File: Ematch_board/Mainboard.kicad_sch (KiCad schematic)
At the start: 73 parts, among them J10 Conn_01x02_Male, J7 Conn_01x06_Female, J8 USB_C_Receptacle_USB2.0, J9 Conn_01x02_Male, Q1 MMDT2222A, Q2 MMDT2222A, U2 LTC4411, U3 RT9025-25GSP, U4 LTC4411, U5 SN65HVD230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

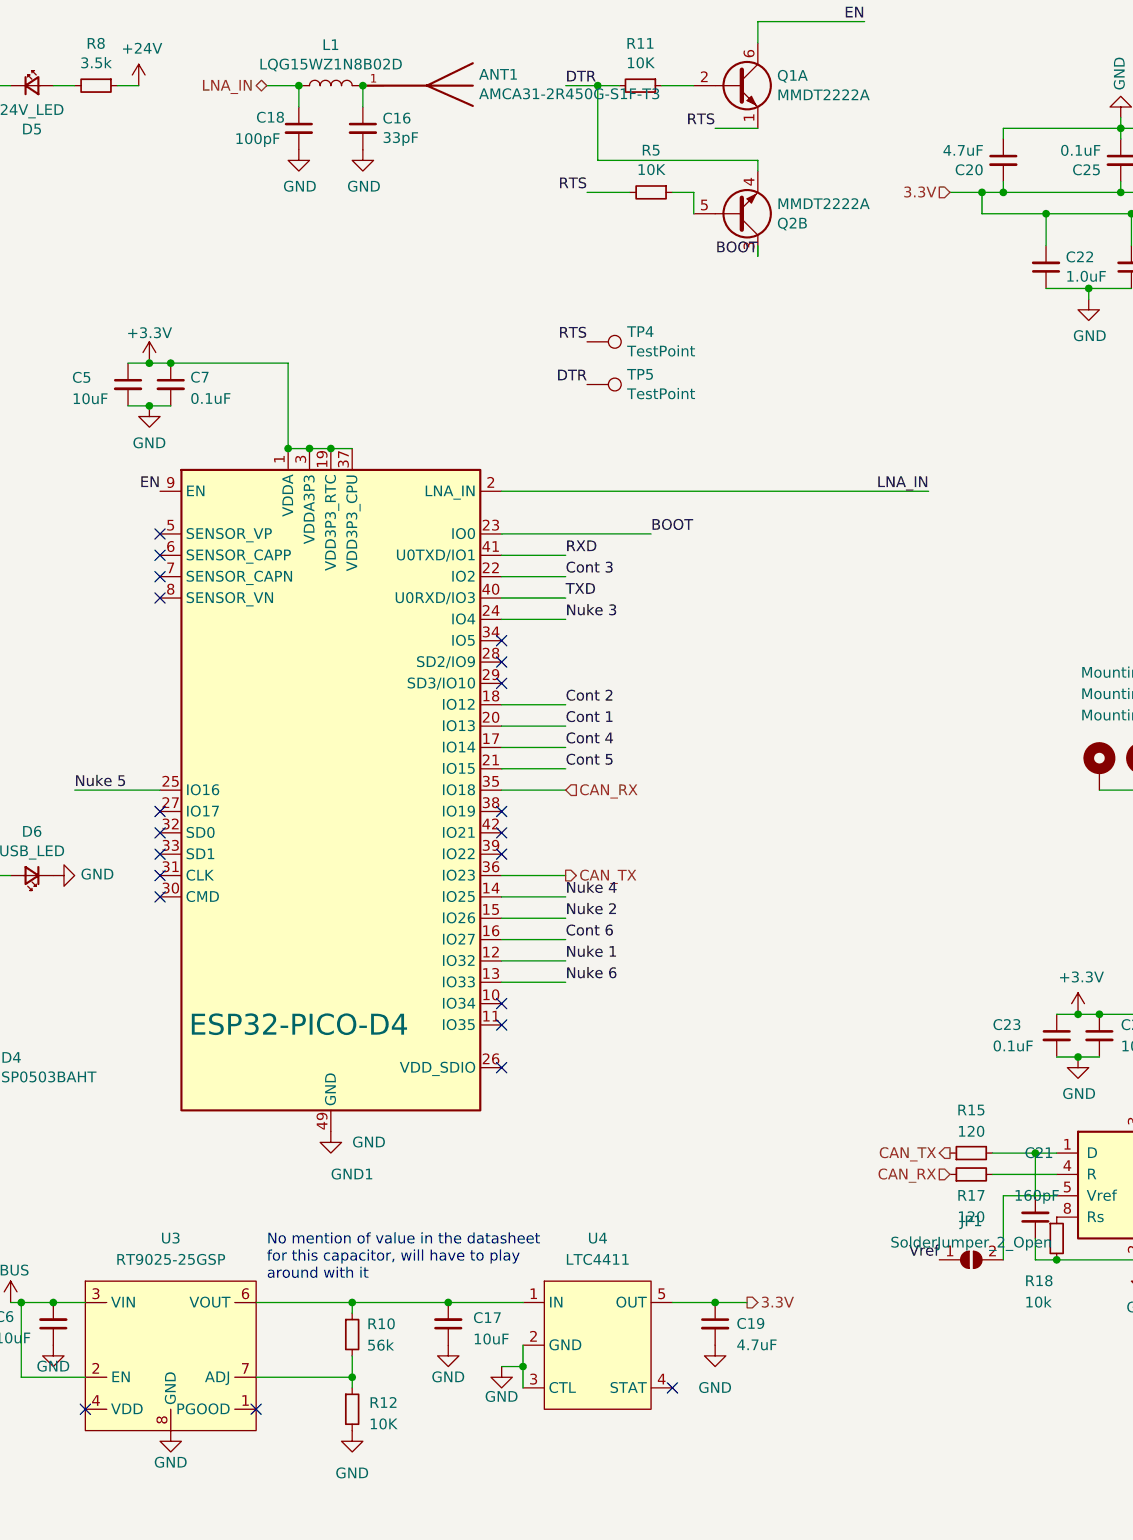
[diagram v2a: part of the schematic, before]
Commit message: routed thicker 24V traces and moved some components
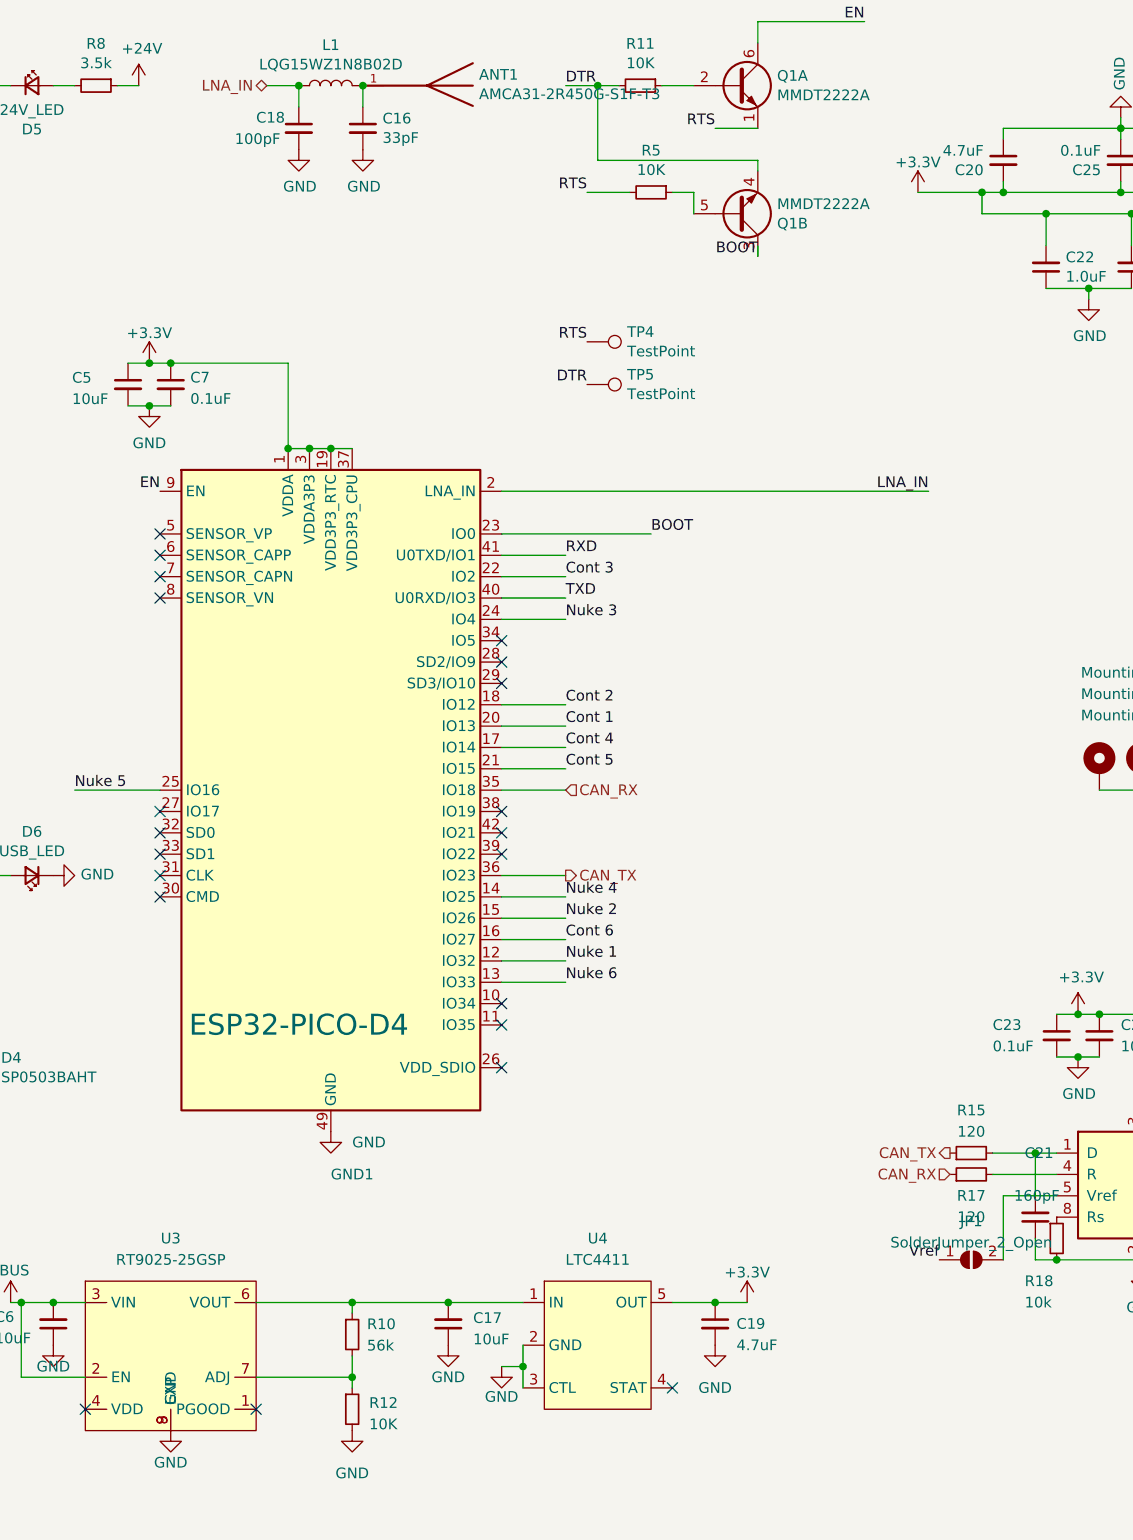
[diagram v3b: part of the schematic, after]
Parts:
- U3: footprint Package_SO:SOP-8_3.9x4.9mm_P1.27mm -> iclr:SOIC127P599X175-9N
- renumbered Q2 to Q1
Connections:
- net 3.3V is gone; now on net +3V3: C19.1, C20.2, C22.2, C25.2, C26.2, U4.5 (OUT), U6.6 (VDD), U6.7 (REGIN)
- net GND: now also U3.9 (EXP)
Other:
- note removed: "No mention of value in the datasheet for this capacitor, will have to play around with it"
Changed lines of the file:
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@@
     (stroke (width 0) (type default) (color 0 0 0 0))
   )
-  (wire (pts (xy 177.8 35.56) (xy 181.61 35.56))
+  (wire (pts (xy 173.99 35.56) (xy 181.61 35.56))
     (stroke (width 0) (type default) (color 0 0 0 0))
   )
@@
     (effects (font (size 2.5 2.5)) (justify left bottom))
   )
-  (text "No mention of value in the datasheet \nfor this capacitor, will have to play\naround with it\n"
-    (at 96.52 165.1 0)
-    (effects (font (size 1.27 1.27)) (justify left bottom))
-  )
   (text "0.1\n\n" (at 269.24 195.58 0)
     (effects (font (size 1.27 1.27)) (justify left bottom))
@@
   )
   (hierarchical_label "CAN_LOW" (shape bidirectional) (at 237.49 162.56 0)
-    (effects (font (size 1.27 1.27)) (justify left))
-  )
-  (hierarchical_label "3.3V" (shape input) (at 177.8 35.56 180)
-    (effects (font (size 1.27 1.27)) (justify right))
-  )
-  (hierarchical_label "3.3V" (shape output) (at 153.67 167.64 0)
     (effects (font (size 1.27 1.27)) (justify left))
   )
@@
     (pin "1")
   )
+  (symbol (lib_id "power:+3.3V") (at 153.67 167.64 0) (unit 1)
+    (in_bom yes) (on_board yes) (fields_autoplaced)
+    (property "Reference" "#PWR0156" (id 0) (at 153.67 171.45 0)
+      (effects (font (size 1.27 1.27)) hide)
+    )
+    (property "Value" "+3.3V" (id 1) (at 153.67 164.0642 0))
+    (property "Footprint" "" (id 2) (at 153.67 167.64 0)
+      (effects (font (size 1.27 1.27)) hide)
+    )
+    (property "Datasheet" "" (id 3) (at 153.67 167.64 0)
+      (effects (font (size 1.27 1.27)) hide)
+    )
+    (pin "1")
+  )
   (symbol (lib_id "Device:C_Small") (at 80.01 58.42 0) (unit 1)
     (in_bom yes) (on_board yes)
@@
     (property "Reference" "U3" (id 0) (at 85.09 160.02 0))
     (property "Value" "RT9025-25GSP" (id 1) (at 85.09 162.56 0))
-    (property "Footprint" "Package_SO:SOP-8_3.9x4.9mm_P1.27mm" (id 2) (at 85.09 161.29 0)
+    (property "Footprint" "iclr:SOIC127P599X175-9N" (id 2) (at 85.09 161.29 0)
       (effects (font (size 1.27 1.27)) hide)
     )
@@
     (pin "7")
     (pin "8")
+    (pin "9")
   )
   (symbol (lib_id "power:+3.3V") (at 39.37 17.78 0) (unit 1)
@@
   (symbol (lib_id "Transistor_BJT:MMDT2222A") (at 152.4 38.1 0) (mirror x) (unit 2)
     (in_bom yes) (on_board yes)
-    (property "Reference" "Q2" (id 0) (at 157.226 39.2684 0)
+    (property "Reference" "Q1" (id 0) (at 157.226 39.2684 0)
       (effects (font (size 1.27 1.27)) (justify left))
     )
@@
     (pin "2")
   )
+  (symbol (lib_id "power:+3.3V") (at 173.99 35.56 0) (unit 1)
+    (in_bom yes) (on_board yes) (fields_autoplaced)
+    (property "Reference" "#PWR0155" (id 0) (at 173.99 39.37 0)
+      (effects (font (size 1.27 1.27)) hide)
+    )
+    (property "Value" "+3.3V" (id 1) (at 173.99 31.9842 0))
+    (property "Footprint" "" (id 2) (at 173.99 35.56 0)
+      (effects (font (size 1.27 1.27)) hide)
+    )
+    (property "Datasheet" "" (id 3) (at 173.99 35.56 0)
+      (effects (font (size 1.27 1.27)) hide)
+    )
+    (pin "1")
+  )
   (symbol (lib_id "Device:LED_Small") (at 25.4 17.78 0) (unit 1)
     (in_bom yes) (on_board yes)
@@
       (reference "#PWR0154") (unit 1) (value "GND") (footprint "")
     )
+    (path "/df5e49c6-770d-49a3-bf1b-c97c8450671f"
+      (reference "#PWR0155") (unit 1) (value "+3.3V") (footprint "")
+    )
+    (path "/46921c1f-bdeb-4788-94e2-0c9bd6035141"
+      (reference "#PWR0156") (unit 1) (value "+3.3V") (footprint "")
+    )
     (path "/3577b5d9-2ff9-467d-ae6e-3ec7e7bc32ec"
       (reference "#PWR0157") (unit 1) (value "GND") (footprint "")
@@
     )
     (path "/980f11b3-8fb5-4dd9-bedf-9b22652526a8"
-      (reference "Q2") (unit 2) (value "MMDT2222A") (footprint "Package_TO_SOT_SMD:SOT-363_SC-70-6")
+      (reference "Q1") (unit 2) (value "MMDT2222A") (footprint "Package_TO_SOT_SMD:SOT-363_SC-70-6")
     )
     (path "/00000000-0000-0000-0000-000061c80f8f/2fdb32e7-7db5-44a9-bdec-28eee95a9760"
@@
     )
     (path "/79f9859b-6f0f-4b8d-bc64-43efc8037e4c"
-      (reference "U3") (unit 1) (value "RT9025-25GSP") (footprint "Package_SO:SOP-8_3.9x4.9mm_P1.27mm")
+      (reference "U3") (unit 1) (value "RT9025-25GSP") (footprint "iclr:SOIC127P599X175-9N")
     )
     (path "/f4b8df4e-cc6e-426d-b25b-296487d3b549"

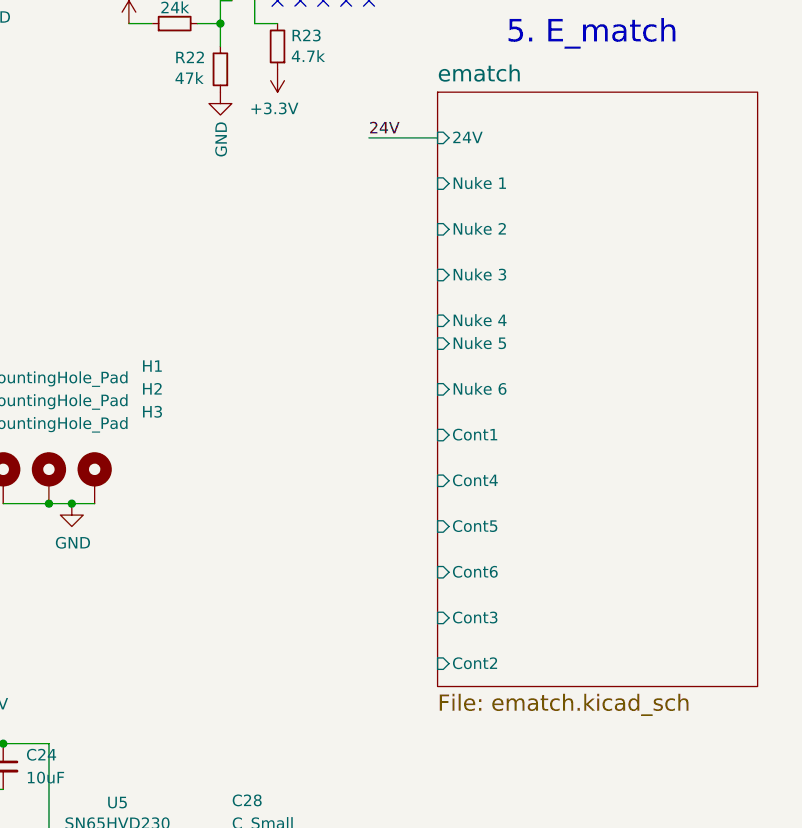
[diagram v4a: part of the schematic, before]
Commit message: completed layout for screw terminals, moved some LEDs
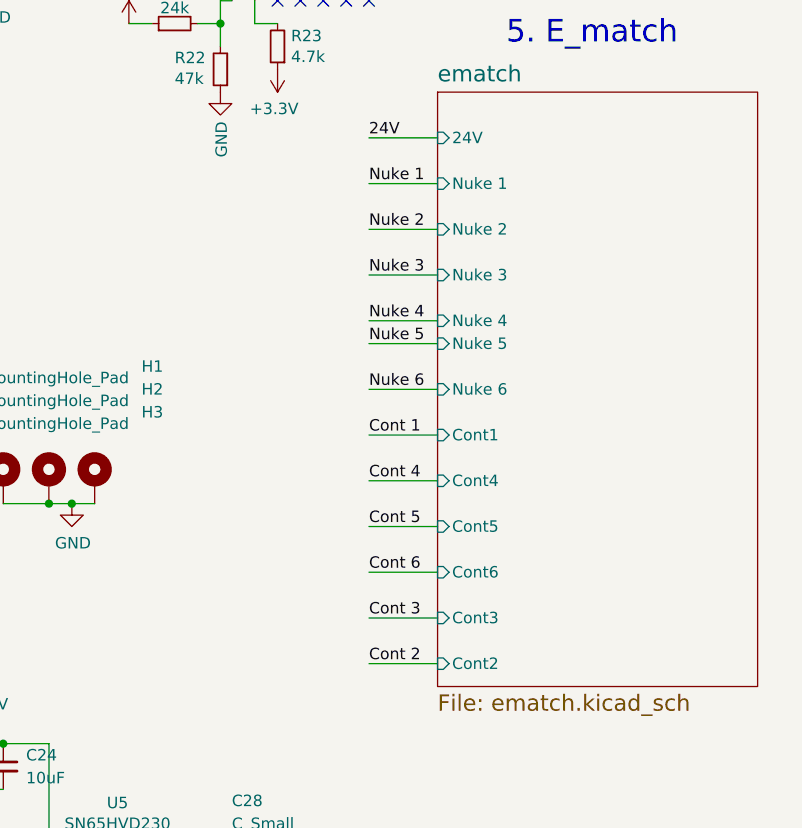
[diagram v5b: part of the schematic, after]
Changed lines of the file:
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@@
+    (stroke (width 0) (type default) (color 0 0 0 0))
+  )
+  (wire (pts (xy 236.22 76.2) (xy 243.84 76.2))
     (stroke (width 0) (type default) (color 0 0 0 0))
   )
@@
     (stroke (width 0) (type default) (color 0 0 0 0))
   )
+  (wire (pts (xy 236.22 124.46) (xy 243.84 124.46))
+    (stroke (width 0) (type default) (color 0 0 0 0))
+  )
   (wire (pts (xy 106.68 167.64) (xy 106.68 168.91))
     (stroke (width 0) (type default) (color 0 0 0 0))
@@
     (stroke (width 0) (type default) (color 0 0 0 0))
   )
+  (wire (pts (xy 236.22 104.14) (xy 243.84 104.14))
+    (stroke (width 0) (type default) (color 0 0 0 0))
+  )
   (wire (pts (xy -12.7 101.6) (xy -5.08 101.6))
     (stroke (width 0) (type default) (color 0 0 0 0))
@@
     (stroke (width 0) (type default) (color 0 0 0 0))
   )
+  (wire (pts (xy 236.22 93.98) (xy 243.84 93.98))
+    (stroke (width 0) (type default) (color 0 0 0 0))
+  )
   (wire (pts (xy 226.06 10.16) (xy 226.06 2.54))
     (stroke (width 0) (type default) (color 0 0 0 0))
   )
+  (wire (pts (xy 236.22 81.28) (xy 243.84 81.28))
+    (stroke (width 0) (type default) (color 0 0 0 0))
+  )
   (wire (pts (xy 124.46 116.84) (xy 132.08 116.84))
     (stroke (width 0) (type default) (color 0 0 0 0))
@@
     (stroke (width 0) (type default) (color 0 0 0 0))
   )
+  (wire (pts (xy 236.22 88.9) (xy 243.84 88.9))
+    (stroke (width 0) (type default) (color 0 0 0 0))
+  )
   (wire (pts (xy -15.24 40.64) (xy -7.62 40.64))
     (stroke (width 0) (type default) (color 0 0 0 0))
@@
     (stroke (width 0) (type default) (color 0 0 0 0))
   )
+  (wire (pts (xy 236.22 71.12) (xy 243.84 71.12))
+    (stroke (width 0) (type default) (color 0 0 0 0))
+  )
   (wire (pts (xy 17.78 17.78) (xy 22.86 17.78))
     (stroke (width 0) (type default) (color 0 0 0 0))
@@
     (stroke (width 0) (type default) (color 0 0 0 0))
   )
+  (wire (pts (xy 236.22 114.3) (xy 243.84 114.3))
+    (stroke (width 0) (type default) (color 0 0 0 0))
+  )
   (wire (pts (xy 15.24 149.86) (xy 16.51 149.86))
     (stroke (width 0) (type default) (color 0 0 0 0))
@@
     (stroke (width 0) (type default) (color 0 0 0 0))
   )
+  (wire (pts (xy 236.22 109.22) (xy 243.84 109.22))
+    (stroke (width 0) (type default) (color 0 0 0 0))
+  )
   (wire (pts (xy 124.46 86.36) (xy 132.08 86.36))
     (stroke (width 0) (type default) (color 0 0 0 0))
@@
     (stroke (width 0) (type default) (color 0 0 0 0))
   )
+  (wire (pts (xy 236.22 99.06) (xy 243.84 99.06))
+    (stroke (width 0) (type default) (color 0 0 0 0))
+  )
   (wire (pts (xy -12.7 5.08) (xy -12.7 10.16))
     (stroke (width 0) (type default) (color 0 0 0 0))
@@
     (stroke (width 0) (type default) (color 0 0 0 0))
   )
+  (wire (pts (xy 236.22 86.36) (xy 243.84 86.36))
+    (stroke (width 0) (type default) (color 0 0 0 0))
+  )
   (wire (pts (xy 199.39 41.91) (xy 199.39 38.1))
+    (stroke (width 0) (type default) (color 0 0 0 0))
+  )
+  (wire (pts (xy 236.22 119.38) (xy 243.84 119.38))
     (stroke (width 0) (type default) (color 0 0 0 0))
   )
@@
     (effects (font (size 1.27 1.27)) (justify left bottom))
   )
+  (label "Nuke 1" (at 236.22 71.12 0)
+    (effects (font (size 1.27 1.27)) (justify left bottom))
+  )
   (label "BOOT" (at 10.16 45.72 0)
     (effects (font (size 1.27 1.27)) (justify left bottom))
@@
     (effects (font (size 1.27 1.27)) (justify left bottom))
   )
+  (label "Cont 2" (at 236.22 124.46 0)
+    (effects (font (size 1.27 1.27)) (justify left bottom))
+  )
   (label "CAN_LOW" (at 26.67 149.86 270)
     (effects (font (size 1.27 1.27)) (justify right bottom))
   )
+  (label "Nuke 5" (at 236.22 88.9 0)
+    (effects (font (size 1.27 1.27)) (justify left bottom))
+  )
   (label "Data+" (at 200.66 30.48 0)
     (effects (font (size 1.27 1.27)) (justify left bottom))
@@
     (effects (font (size 1.27 1.27)) (justify left bottom))
   )
+  (label "Cont 3" (at 236.22 119.38 0)
+    (effects (font (size 1.27 1.27)) (justify left bottom))
+  )
   (label "EN" (at 1.27 15.24 0)
     (effects (font (size 1.27 1.27)) (justify left bottom))
@@
     (effects (font (size 1.27 1.27)) (justify right bottom))
   )
+  (label "Cont 6" (at 236.22 114.3 0)
+    (effects (font (size 1.27 1.27)) (justify left bottom))
+  )
   (label "VBUS" (at 57.15 134.62 90)
     (effects (font (size 1.27 1.27)) (justify left bottom))
@@
     (effects (font (size 1.27 1.27)) (justify left bottom))
   )
+  (label "Cont 4" (at 236.22 104.14 0)
+    (effects (font (size 1.27 1.27)) (justify left bottom))
+  )
   (label "Cont 6" (at 132.08 124.46 0)
     (effects (font (size 1.27 1.27)) (justify left bottom))
@@
     (effects (font (size 1.27 1.27)) (justify right bottom))
   )
+  (label "Nuke 2" (at 236.22 76.2 0)
+    (effects (font (size 1.27 1.27)) (justify left bottom))
+  )
   (label "Data-" (at 200.66 33.02 0)
     (effects (font (size 1.27 1.27)) (justify left bottom))
@@
     (effects (font (size 1.27 1.27)) (justify right bottom))
   )
+  (label "Nuke 6" (at 236.22 93.98 0)
+    (effects (font (size 1.27 1.27)) (justify left bottom))
+  )
   (label "Cont 5" (at 132.08 104.14 0)
     (effects (font (size 1.27 1.27)) (justify left bottom))
@@
     (effects (font (size 1.27 1.27)) (justify left bottom))
   )
+  (label "Cont 1" (at 236.22 99.06 0)
+    (effects (font (size 1.27 1.27)) (justify left bottom))
+  )
   (label "Vref" (at 215.9 153.67 180)
     (effects (font (size 1.27 1.27)) (justify right bottom))
@@
     (effects (font (size 1.27 1.27)) (justify right bottom))
   )
+  (label "Cont 5" (at 236.22 109.22 0)
+    (effects (font (size 1.27 1.27)) (justify left bottom))
+  )
+  (label "Nuke 4" (at 236.22 86.36 0)
+    (effects (font (size 1.27 1.27)) (justify left bottom))
+  )
   (label "CAN_HIGH" (at 24.13 149.86 270)
     (effects (font (size 1.27 1.27)) (justify right bottom))
@@
     (effects (font (size 1.27 1.27)) (justify left bottom))
   )
+  (label "Nuke 3" (at 236.22 81.28 0)
+    (effects (font (size 1.27 1.27)) (justify left bottom))
+  )

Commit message: initial routing of cont and nuke traces
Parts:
- J7: value Conn_01x06_Female -> RBUS
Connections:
- net Cont 1: now also GND1.30 (CMD); no longer GND1.20 (IO13)
- net Cont 2: now also GND1.29 (SD3/IO10); no longer GND1.18 (IO12)
- net Cont 3: now also GND1.31 (CLK); no longer GND1.22 (IO2)
- net Cont 4: now also GND1.28 (SD2/IO9); no longer GND1.17 (IO14)
- net Nuke 1: now also GND1.32 (SD0); no longer GND1.12 (IO32)
- net Nuke 3: now also GND1.33 (SD1); no longer GND1.24 (IO4)
- net Nuke 5: now also GND1.34 (IO5); no longer GND1.25 (IO16)
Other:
- moved on the sheet: D6, R7
